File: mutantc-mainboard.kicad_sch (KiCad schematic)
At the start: 24 parts, among them J1 Conn_01x16, J2 Conn_01x10, J3 Conn_02x10_Odd_Even, J4 Conn_02x20_Odd_Even, J5 USB_C_Receptacle_USB2.0_16P, J6 USB_C_Receptacle_USB2.0_16P, J7 Conn_02x04_Odd_Even, U1 DS3231MZ, U2 ESP32-S2-WROVER, U3 TP4056

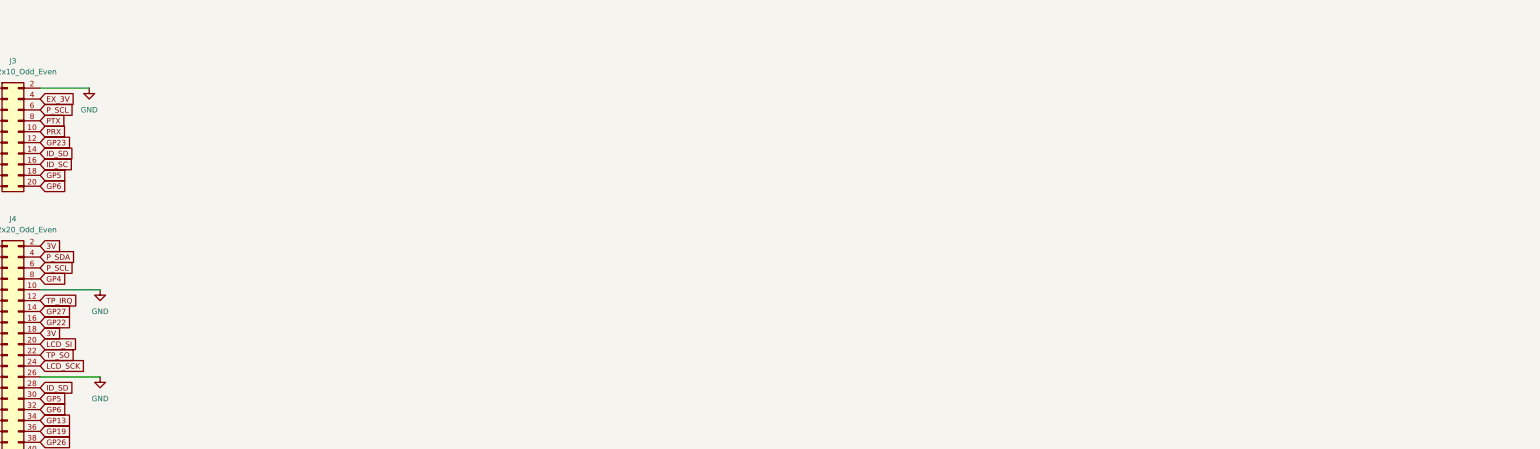
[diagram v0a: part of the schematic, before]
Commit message: Added keyboard matrix to main
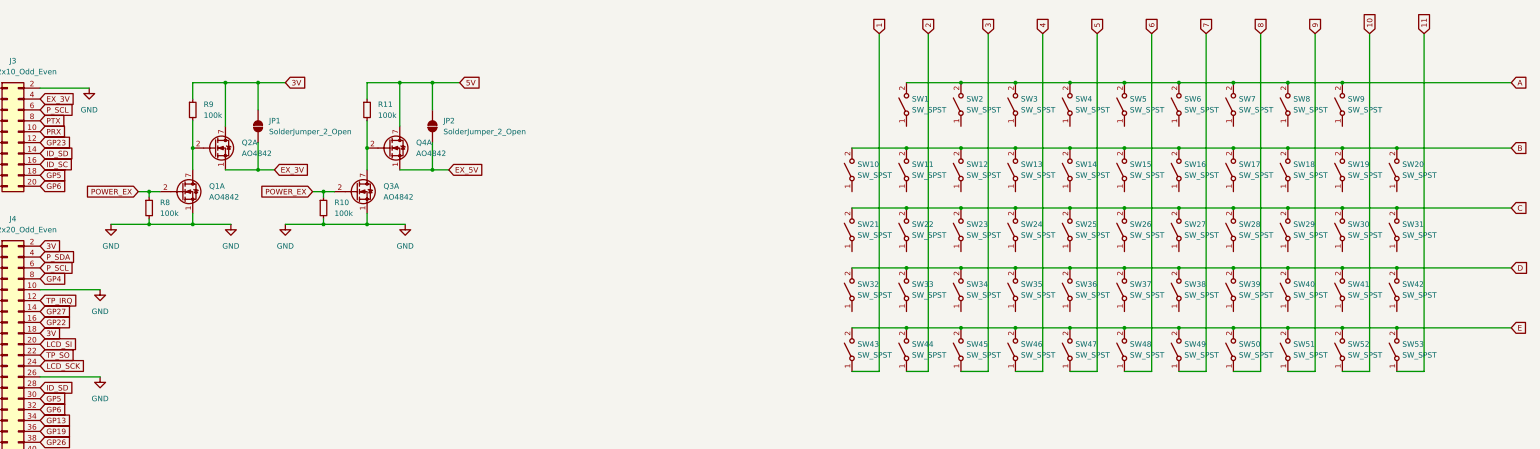
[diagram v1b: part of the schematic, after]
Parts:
- added JP1, JP2: SolderJumper_2_Open, Jumper:SolderJumper-2_P1.3mm_Open_RoundedPad1.0x1.5mm, symbol Jumper:SolderJumper_2_Open
- added Q1, Q2, Q3, Q4: AO4842, Package_SO:SOIC-8_3.9x4.9mm_P1.27mm, symbol Transistor_FET:AO4842
- added R10, R11, R8, R9: 100k, Resistor_SMD:R_1206_3216Metric, symbol Device:R_Small
- added SW1, SW10, SW11, SW12, SW13, SW14, SW15, SW16, SW17, SW18, SW19, SW2, SW20, SW21, SW22, SW23, SW24, SW25, SW26, SW27, SW28, SW29, SW3, SW30, SW31, SW32, SW33, SW34, SW35, SW36, SW37, SW38, SW39, SW4, SW40, SW41, SW42, SW43, SW44, SW45, SW46, SW47, SW48, SW49, SW5, SW50, SW51, SW52, SW53, SW6, SW7, SW8, SW9: SW_SPST, symbol Switch:SW_SPST
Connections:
- net 1: now also SW43.1 (A)
- net 10: now also SW52.1 (A)
- net 11: now also SW53.1 (A)
- net 2: now also SW44.1 (A)
- net 3: now also SW45.1 (A)
- net 3V: now also JP1.2 (B), Q2.7 (D1), Q2.8 (D1), R9.1
- net 4: now also SW46.1 (A)
- net 5: now also SW47.1 (A)
- net 5V: now also JP2.2 (B), Q4.7 (D1), Q4.8 (D1), R11.1
- net 6: now also SW48.1 (A)
- net 7: now also SW49.1 (A)
- net 8: now also SW50.1 (A)
- net 9: now also SW51.1 (A)
- net A: now also SW1.2 (B), SW2.2 (B), SW3.2 (B), SW4.2 (B), SW5.2 (B), SW6.2 (B), SW7.2 (B), SW8.2 (B), SW9.2 (B)
- net B: now also SW10.2 (B), SW11.2 (B), SW12.2 (B), SW13.2 (B), SW14.2 (B), SW15.2 (B), SW16.2 (B), SW17.2 (B), SW18.2 (B), SW19.2 (B), SW20.2 (B)
- net C: now also SW21.2 (B), SW22.2 (B), SW23.2 (B), SW24.2 (B), SW25.2 (B), SW26.2 (B), SW27.2 (B), SW28.2 (B), SW29.2 (B), SW30.2 (B), SW31.2 (B)
- net D: now also SW32.2 (B), SW33.2 (B), SW34.2 (B), SW35.2 (B), SW36.2 (B), SW37.2 (B), SW38.2 (B), SW39.2 (B), SW40.2 (B), SW41.2 (B), SW42.2 (B)
- net E: now also SW43.2 (B), SW44.2 (B), SW45.2 (B), SW46.2 (B), SW47.2 (B), SW48.2 (B), SW49.2 (B), SW50.2 (B), SW51.2 (B), SW52.2 (B), SW53.2 (B)
- net EX_3V: now also JP1.1 (A), Q2.1 (S1)
- net EX_5V: now also JP2.1 (A), Q4.1 (S1)
- net GND: now also Q1.1 (S1), Q3.1 (S1), R10.2, R8.2
- net POWER_EX: now also Q1.2 (G1), Q3.2 (G1), R10.1, R8.1
- new net: Q3.7 (D1), Q3.8 (D1), Q4.2 (G1), R11.2
- new net: Q1.7 (D1), Q1.8 (D1), Q2.2 (G1), R9.2
